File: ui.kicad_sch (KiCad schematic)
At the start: 0 parts

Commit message: Finish first design
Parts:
- added BZ1: AST1109MLTRQ, Buzzer_Beeper:Buzzer_Mallory_AST1109MLTRQ, symbol Device:Buzzer
- added C15, C17, C18: 100n, Capacitor_SMD:C_0603_1608Metric, symbol Device:C
- added Q11: IRLML2502, Package_TO_SOT_SMD:SOT-23, symbol Device:Q_NMOS_GSD
- added R32: R120, Resistor_SMD:R_0805_2012Metric, symbol Device:R
- added R33, R34, R35, R36: R100k, Resistor_SMD:R_0805_2012Metric, symbol Device:R
- added R37, R39, R40: 1k, Resistor_SMD:R_0603_1608Metric, symbol Device:R
- added SW1, SW2, SW3: SW_Push, Button_Switch_SMD:SW_SPST_TL3305A, symbol Switch:SW_Push
- added TP1, TP2, TP3, TP4: TestPoint_Small, TestPoint:TestPoint_Pad_D1.5mm, symbol Connector:TestPoint_Small
- added U8: ~, project:OLED_1.5in_128x128, symbol project:OLED_1.5in_128x128
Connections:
- new net: R39.1, SW2.1
- new net: R40.1, SW3.1
- new net: R37.1, SW1.1
- new net +3.3V: SW1.2, SW2.2, SW3.2, TP1.1, U8.1 (VCC)
- new net +5V: BZ1.1 (+)
- new net BUTTON_1: C15.1, R34.2, R37.2
- new net BUTTON_2: C17.1, R35.2, R39.2
- new net BUTTON_3: C18.1, R36.2, R40.2
- new net BUZZER: R32.1
- new net BUZZER_GATE: Q11.1 (G), R32.2, R33.2
- new net BUZZER_GND: BZ1.2 (-), Q11.3 (D)
- new net GND: C15.2, C17.2, C18.2, Q11.2 (S), R33.1, R34.1, R35.1, R36.1, TP2.1, U8.2 (GND)
- new net OLED_SCL: TP3.1, U8.3 (SCL)
- new net OLED_SDA: TP4.1, U8.4 (SDA)
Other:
- note added: "Buttons"
- note added: "Buzzer"
- note added: "I2C Display"
- title: (none) -> openautolab - Mainboard

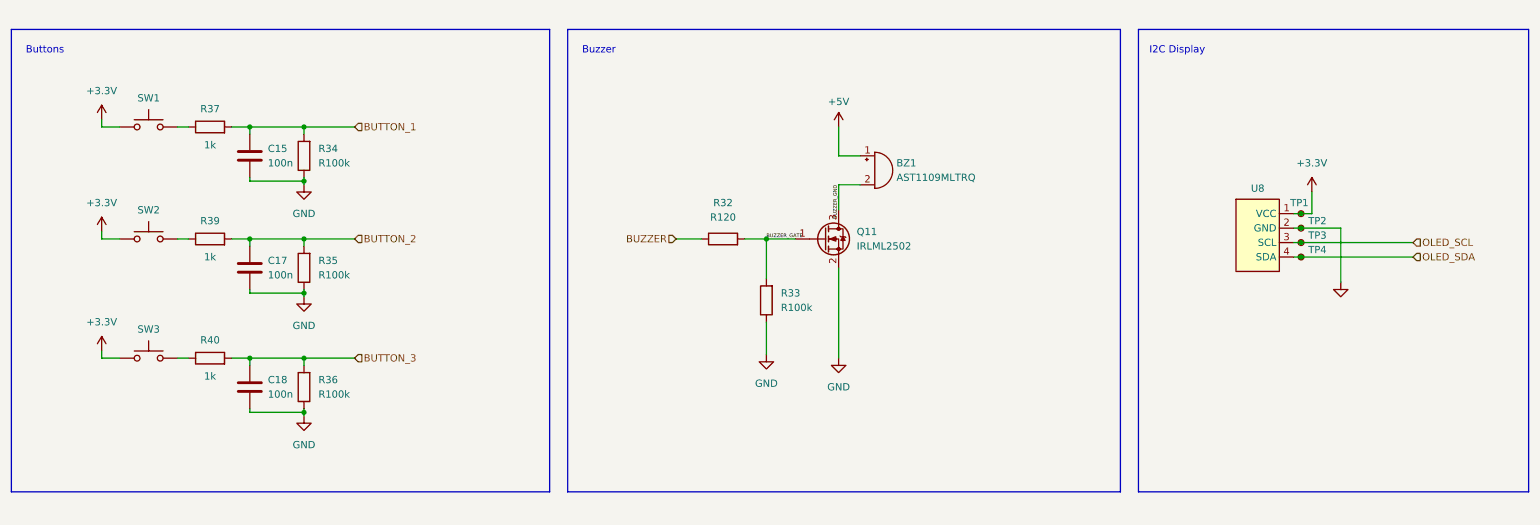
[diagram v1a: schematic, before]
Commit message: Add screen FPC to schematic and remove old OLED stuff
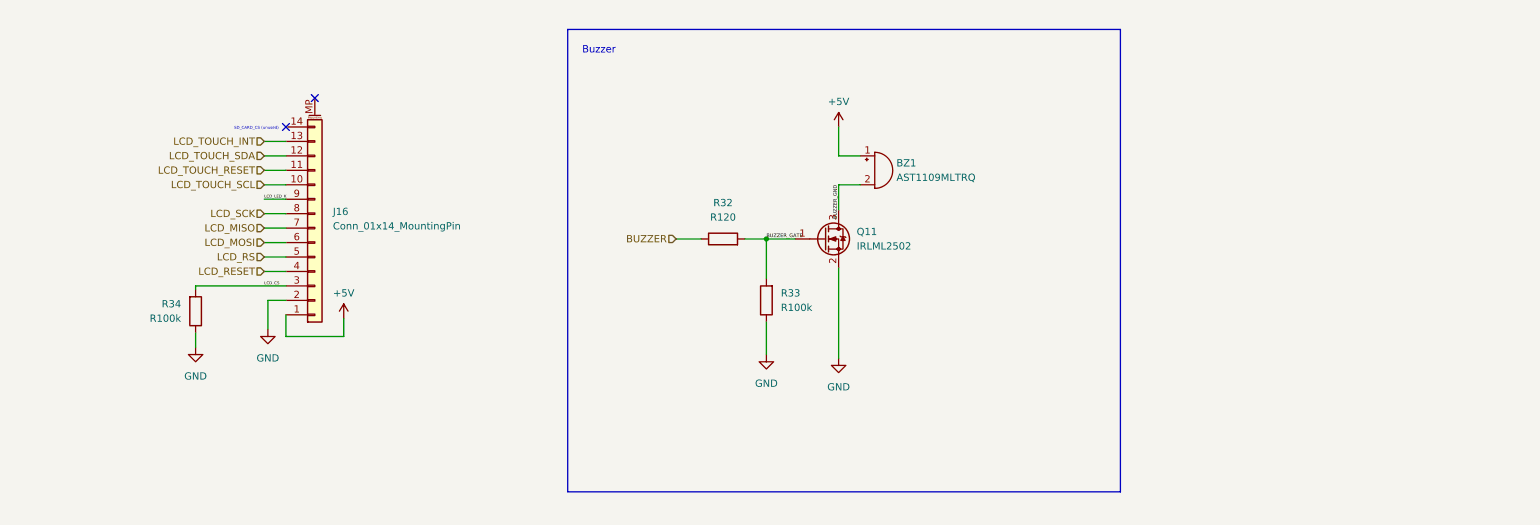
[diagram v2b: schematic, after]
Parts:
- removed C15, C17, C18: 100n, Capacitor_SMD:C_0603_1608Metric, symbol Device:C
- removed R35, R36: R100k, Resistor_SMD:R_0805_2012Metric, symbol Device:R
- removed R37, R39, R40: 1k, Resistor_SMD:R_0603_1608Metric, symbol Device:R
- removed SW1, SW2, SW3: SW_Push, Button_Switch_SMD:SW_SPST_TL3305A, symbol Switch:SW_Push
- removed TP1, TP2, TP3, TP4: TestPoint_Small, TestPoint:TestPoint_Pad_D1.5mm, symbol Connector:TestPoint_Small
- removed U8: ~, project:OLED_1.5in_128x128, symbol project:OLED_1.5in_128x128
- added J16: Conn_01x14_MountingPin, Connector_FFC-FPC:TE_1-1734839-4_1x14-1MP_P0.5mm_Horizontal, symbol Connector_Generic_MountingPin:Conn_01x14_MountingPin
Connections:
- net +5V: now also J16.1 (Pin_1)
- net GND: now also J16.2 (Pin_2)
- net BUTTON_1 renamed LCD_CS
- net LCD_CS: now also J16.3 (Pin_3)
- new net LCD_LED_K: J16.9 (Pin_9)
- new net LCD_MISO: J16.7 (Pin_7)
- new net LCD_MOSI: J16.6 (Pin_6)
- new net LCD_RESET: J16.4 (Pin_4)
- new net LCD_RS: J16.5 (Pin_5)
- new net LCD_SCK: J16.8 (Pin_8)
- new net LCD_TOUCH_INT: J16.13 (Pin_13)
- new net LCD_TOUCH_RESET: J16.11 (Pin_11)
- new net LCD_TOUCH_SCL: J16.10 (Pin_10)
- new net LCD_TOUCH_SDA: J16.12 (Pin_12)
- no-connect marks 0 -> 2
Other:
- note added: "SD_CARD_CS (unused)"
- note removed: "Buttons"
- note removed: "I2C Display"
- moved on the sheet: R34

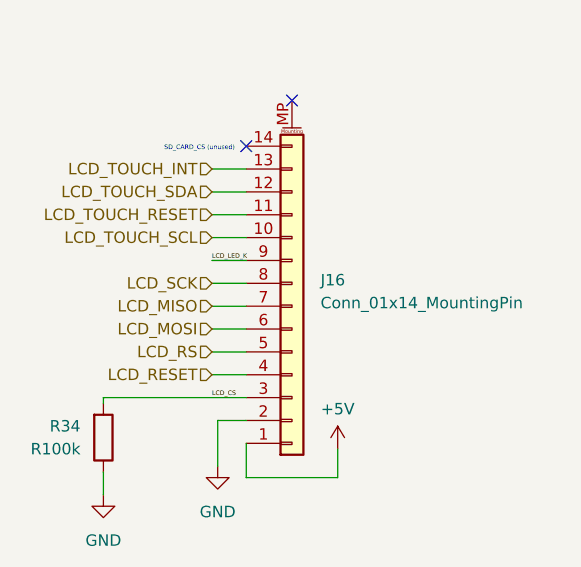
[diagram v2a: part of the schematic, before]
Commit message: Fix LCD connector pin mapping and map them to MCU pins
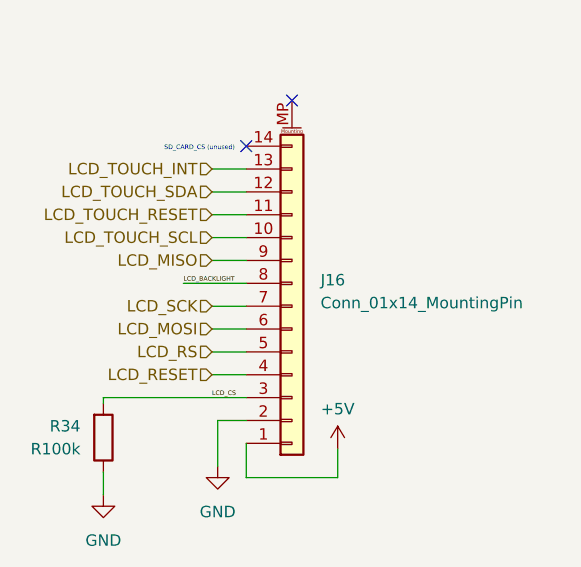
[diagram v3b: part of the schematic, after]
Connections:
- net LCD_LED_K is gone; now on net LCD_MISO: J16.9 (Pin_9)
- net LCD_MISO: no longer J16.7 (Pin_7)
- net LCD_SCK: now also J16.7 (Pin_7); no longer J16.8 (Pin_8)
- new net LCD_BACKLIGHT: J16.8 (Pin_8)
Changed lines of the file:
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@@
     (stroke (width 0) (type default))
   )
-  (wire (pts (xy 59.055 89.535) (xy 62.865 89.535))
+  (wire (pts (xy 59.055 92.075) (xy 62.865 92.075))
     (stroke (width 0) (type default))
   )
@@
     (stroke (width 0) (type default))
   )
-  (wire (pts (xy 59.055 92.075) (xy 62.865 92.075))
+  (wire (pts (xy 59.055 86.995) (xy 62.865 86.995))
     (stroke (width 0) (type default))
   )
@@
     (stroke (width 0) (type default))
   )
-  (wire (pts (xy 59.055 86.995) (xy 62.865 86.995))
+  (wire (pts (xy 55.88 89.535) (xy 62.865 89.535))
     (stroke (width 0) (type default))
   )
@@
     (effects (font (size 0.504 0.504)) (justify left bottom))
   )
-  (label "LCD_LED_K" (at 59.055 86.995 0) (fields_autoplaced)
+  (label "LCD_BACKLIGHT" (at 55.88 89.535 0) (fields_autoplaced)
     (effects (font (size 0.504 0.504)) (justify left bottom))
   )
@@
     (effects (font (size 1.27 1.27)) (justify right))
   )
-  (hierarchical_label "LCD_MISO" (shape input) (at 59.055 92.075 180) (fields_autoplaced)
+  (hierarchical_label "LCD_MISO" (shape input) (at 59.055 86.995 180) (fields_autoplaced)
     (effects (font (size 1.27 1.27)) (justify right))
   )
@@
     (effects (font (size 1.27 1.27)) (justify right))
   )
-  (hierarchical_label "LCD_SCK" (shape input) (at 59.055 89.535 180) (fields_autoplaced)
+  (hierarchical_label "LCD_SCK" (shape input) (at 59.055 92.075 180) (fields_autoplaced)
     (effects (font (size 1.27 1.27)) (justify right))
   )

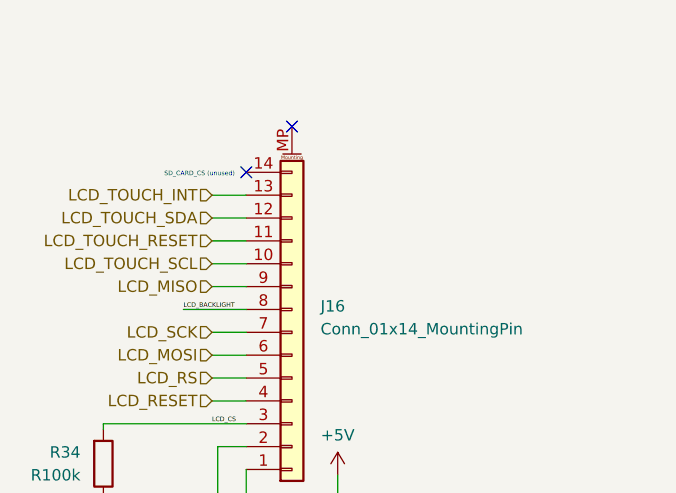
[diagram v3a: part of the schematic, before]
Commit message: Finalize pin mapping, cleanup and layout
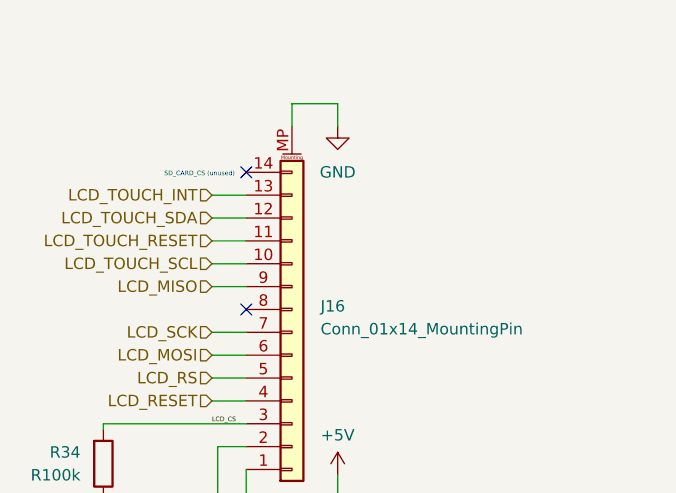
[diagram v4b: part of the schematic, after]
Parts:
- J16: footprint Connector_FFC-FPC:TE_1-1734839-4_1x14-1MP_P0.5mm_Horizontal -> project:XF2M-1415-1A
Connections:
- net GND: now also J16.MP (MountPin)
- net LCD_BACKLIGHT: no longer names the net of J16.8 (Pin_8)
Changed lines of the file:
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@@
   (junction (at 147.32 93.98) (diameter 0) (color 0 0 0 0)
   )
-  (no_connect (at 67.945 69.215))
   (no_connect (at 62.865 74.295))
+  (no_connect (at 62.865 89.535))
+  (wire (pts (xy 67.945 69.215) (xy 67.945 66.675))
+    (stroke (width 0) (type default))
+  )
   (wire (pts (xy 160.02 79.375) (xy 160.02 74.295))
     (stroke (width 0) (type default))
@@
     (stroke (width 0) (type default))
   )
-  (wire (pts (xy 55.88 89.535) (xy 62.865 89.535))
+  (wire (pts (xy 67.945 66.675) (xy 73.025 66.675))
+    (stroke (width 0) (type default))
+  )
+  (wire (pts (xy 73.025 66.675) (xy 73.025 69.215))
     (stroke (width 0) (type default))
   )
@@
   )
   (label "LCD_CS" (at 59.055 102.235 0) (fields_autoplaced)
-    (effects (font (size 0.504 0.504)) (justify left bottom))
-  )
-  (label "LCD_BACKLIGHT" (at 55.88 89.535 0) (fields_autoplaced)
     (effects (font (size 0.504 0.504)) (justify left bottom))
   )
@@
       (effects (font (size 1.27 1.27)) (justify left))
     )
-    (property "Footprint" "Connector_FFC-FPC:TE_1-1734839-4_1x14-1MP_P0.5mm_Horizontal" (at 67.945 92.075 0)
+    (property "Footprint" "project:XF2M-1415-1A" (at 67.945 92.075 0)
       (effects (font (size 1.27 1.27)) hide)
     )
@@
         )
       )
+    )
+  )
+  (symbol (lib_id "power:GND") (at 73.025 69.215 0) (mirror y) (unit 1)
+    (in_bom yes) (on_board yes) (dnp no) (fields_autoplaced)
+    (property "Reference" "#PWR018" (at 73.025 75.565 0)
+      (effects (font (size 1.27 1.27)) hide)
+    )
+    (property "Value" "GND" (at 73.025 74.295 0)
+      (effects (font (size 1.27 1.27)))
+    )
+    (property "Footprint" "" (at 73.025 69.215 0)
+      (effects (font (size 1.27 1.27)) hide)
+    )
+    (property "Datasheet" "" (at 73.025 69.215 0)
+      (effects (font (size 1.27 1.27)) hide)
+    )
+    (pin "1")
+    (instances
+      (project "mainboard"
+        (path "/613f8c39-c37c-4981-8911-5138d36a7959/e16aa466-f341-4735-929a-c85f813defce"
+          (reference "#PWR018") (unit 1)
+        )
+      )

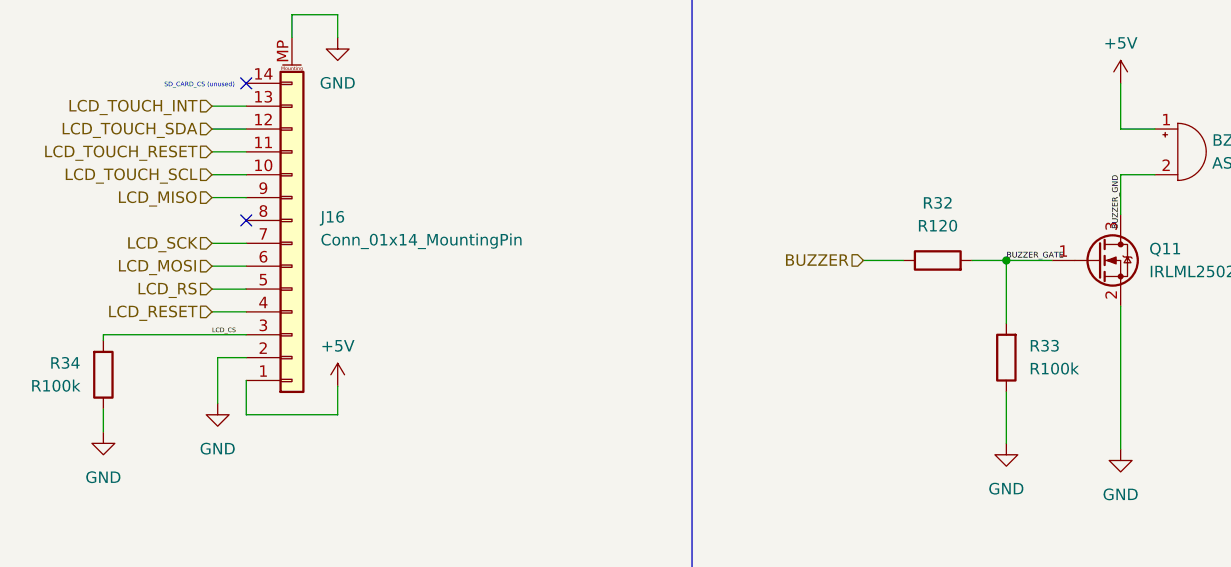
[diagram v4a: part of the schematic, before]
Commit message: Re-annotate parts by board
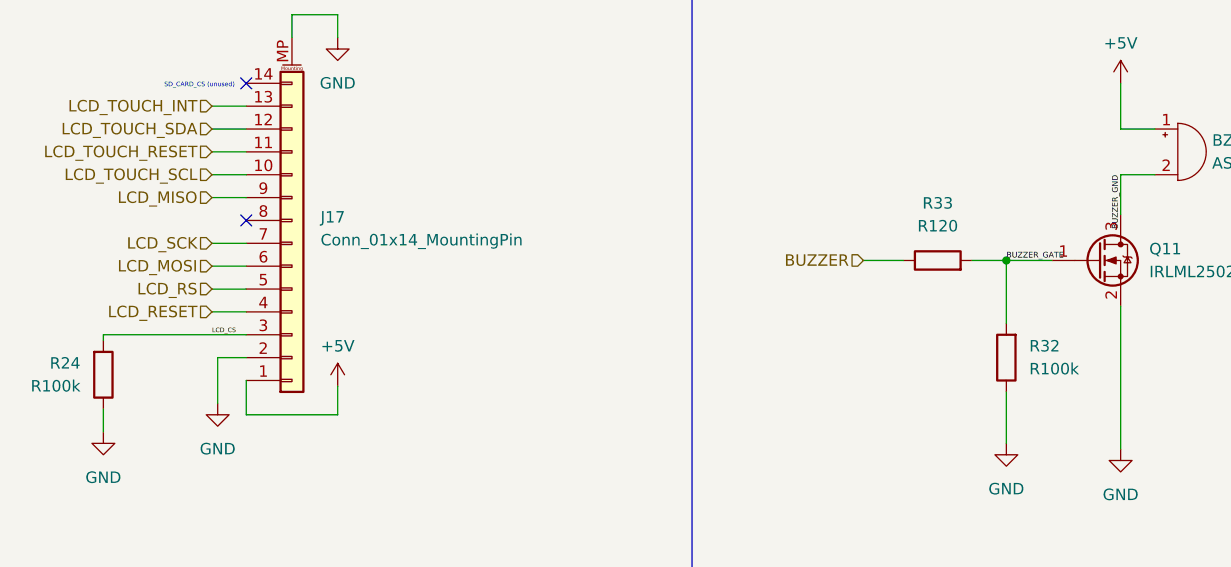
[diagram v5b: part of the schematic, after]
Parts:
- renumbered J16 to J17, R34 to R24, R33 to R32, R32 to R33
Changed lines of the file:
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@@
   (symbol (lib_id "Device:R") (at 147.32 104.775 180) (unit 1)
     (in_bom yes) (on_board yes) (dnp no) (fields_autoplaced)
-    (property "Reference" "R33" (at 149.86 103.505 0)
+    (property "Reference" "R32" (at 149.86 103.505 0)
       (effects (font (size 1.27 1.27)) (justify right))
     )
@@
       (project "mainboard"
         (path "/613f8c39-c37c-4981-8911-5138d36a7959/e16aa466-f341-4735-929a-c85f813defce"
-          (reference "R33") (unit 1)
+          (reference "R32") (unit 1)
         )
       )
@@
   (symbol (lib_id "Device:R") (at 46.99 106.68 0) (mirror x) (unit 1)
     (in_bom yes) (on_board yes) (dnp no)
-    (property "Reference" "R34" (at 44.45 105.41 0)
+    (property "Reference" "R24" (at 44.45 105.41 0)
       (effects (font (size 1.27 1.27)) (justify right))
     )
@@
       (project "mainboard"
         (path "/613f8c39-c37c-4981-8911-5138d36a7959/e16aa466-f341-4735-929a-c85f813defce"
-          (reference "R34") (unit 1)
+          (reference "R24") (unit 1)
         )
       )
@@
   (symbol (lib_id "Device:R") (at 139.7 93.98 90) (unit 1)
     (in_bom yes) (on_board yes) (dnp no) (fields_autoplaced)
-    (property "Reference" "R32" (at 139.7 87.63 90)
+    (property "Reference" "R33" (at 139.7 87.63 90)
       (effects (font (size 1.27 1.27)))
     )
@@
       (project "mainboard"
         (path "/613f8c39-c37c-4981-8911-5138d36a7959/e16aa466-f341-4735-929a-c85f813defce"
-          (reference "R32") (unit 1)
+          (reference "R33") (unit 1)
         )
       )
@@
   (symbol (lib_id "Connector_Generic_MountingPin:Conn_01x14_MountingPin") (at 67.945 92.075 0) (mirror x) (unit 1)
     (in_bom yes) (on_board yes) (dnp no) (fields_autoplaced)
-    (property "Reference" "J16" (at 71.12 89.1794 0)
+    (property "Reference" "J17" (at 71.12 89.1794 0)
       (effects (font (size 1.27 1.27)) (justify left))
     )
@@
       (project "mainboard"
         (path "/613f8c39-c37c-4981-8911-5138d36a7959/e16aa466-f341-4735-929a-c85f813defce"
-          (reference "J16") (unit 1)
-        )
-      )
+          (reference "J17") (unit 1)
+        )
+      )

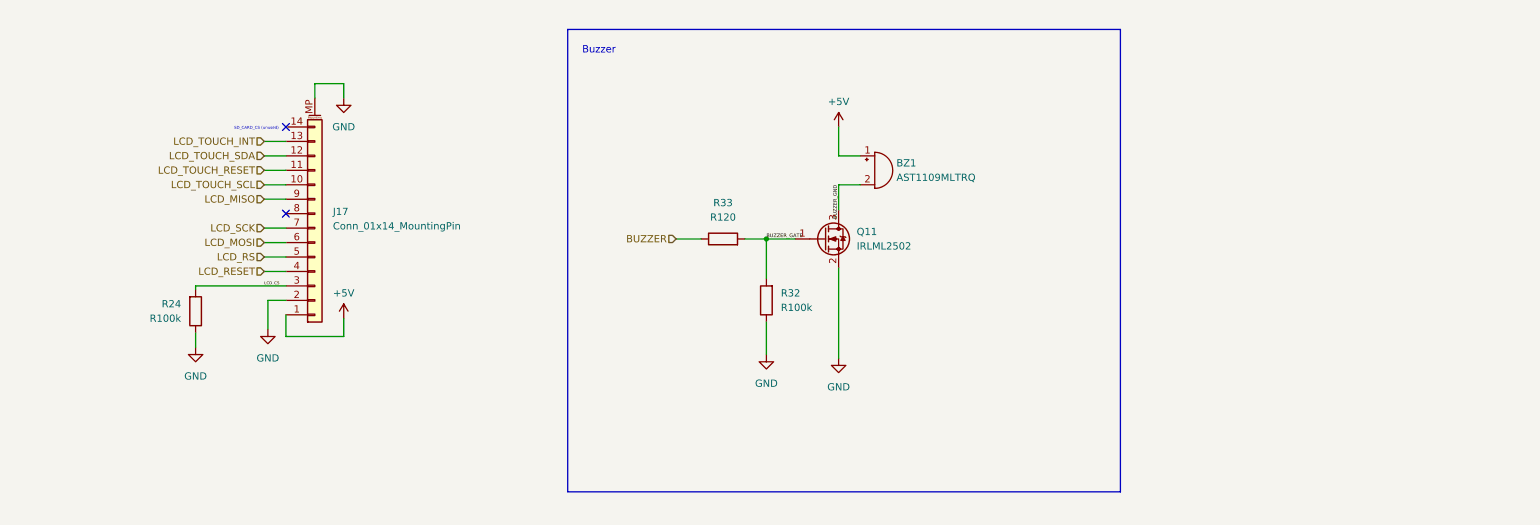
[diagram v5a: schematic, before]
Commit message: Finish integration of TFT interface
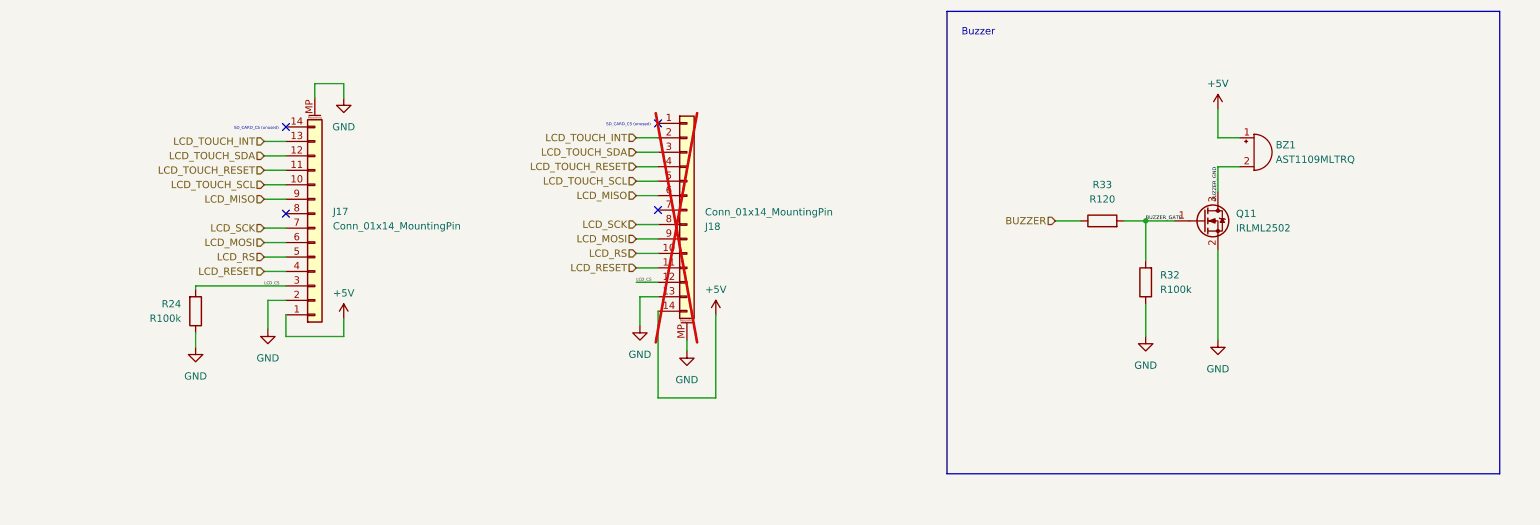
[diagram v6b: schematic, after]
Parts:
- added J18: Conn_01x14_MountingPin, project:XF2M-1415-1A, symbol Connector_Generic_MountingPin:Conn_01x14_MountingPin
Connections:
- net +5V: now also J18.14 (Pin_14)
- net GND: now also J18.13 (Pin_13), J18.MP (MountPin)
- net LCD_CS: now also J18.12 (Pin_12)
- net LCD_MISO: now also J18.6 (Pin_6)
- net LCD_MOSI: now also J18.9 (Pin_9)
- net LCD_RESET: now also J18.11 (Pin_11)
- net LCD_RS: now also J18.10 (Pin_10)
- net LCD_SCK: now also J18.8 (Pin_8)
- net LCD_TOUCH_INT: now also J18.2 (Pin_2)
- net LCD_TOUCH_RESET: now also J18.4 (Pin_4)
- net LCD_TOUCH_SCL: now also J18.5 (Pin_5)
- net LCD_TOUCH_SDA: now also J18.3 (Pin_3)
- no-connect marks 2 -> 4
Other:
- moved on the sheet: BZ1, Q11, R32, R33
